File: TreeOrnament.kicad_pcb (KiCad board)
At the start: 2 copper layers, 80 x 99 mm, 44 parts, among them J1 USB_B_Micro

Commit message: Use newer version of Micro B footprint.
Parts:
- J1: footprint myLibrary:USB_Micro-B_Wuerth-614105150721_CircularHoles -> myLibrary:USB_Micro-B_Wuerth-614105150721_Vertical_CircularHoles

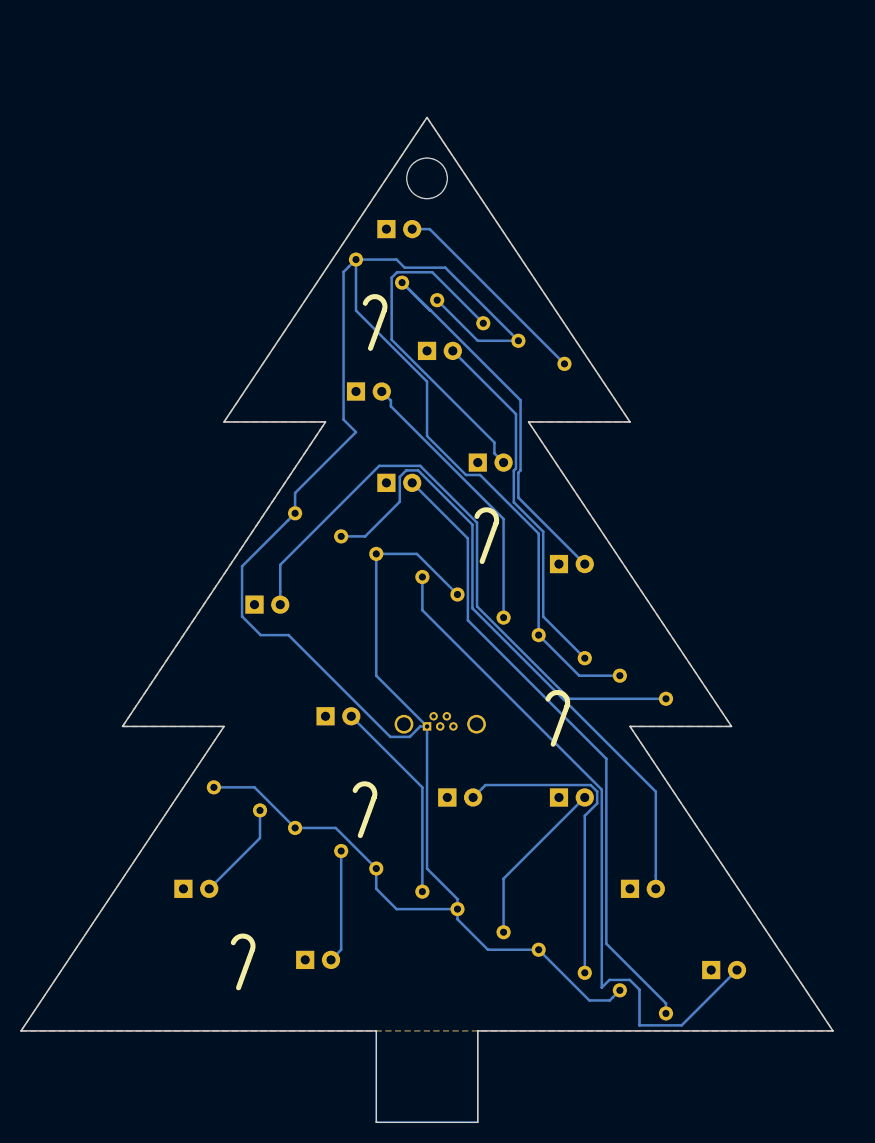
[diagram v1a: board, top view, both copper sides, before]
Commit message: Flip the board over.
(This way the customer ID will be on the "back" instead of the "front".)
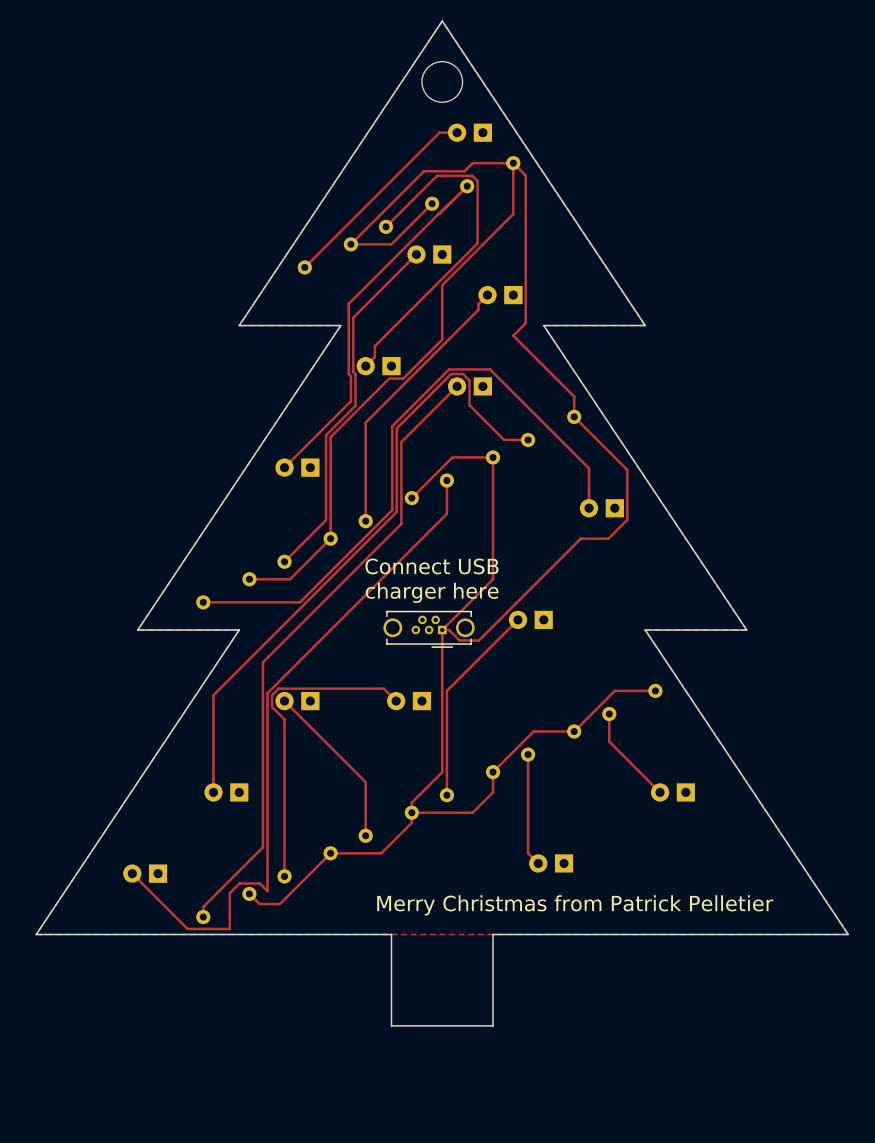
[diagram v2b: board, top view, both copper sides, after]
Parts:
- D1, D10, D11, D12, D13, D14, D2, D3, D4, D5, D6, D7, D8, D9, R1, R10, R11, R12, R13, R14, R2, R3, R4, R5, R6, R7, R8, R9, REF** (x15): moved to B.Cu
- J1: moved to F.Cu
- moved REF** 60.3 mm to (165.5, 105.5), turned to 180 degrees
- moved D8 55.3 mm to (108.5, 104.5), turned to 180 degrees
- moved D1 50.4 mm to (160.5, 96.5), turned to 180 degrees
- moved R1 44.5 mm to (157.5, 86.5), turned to 206.6 degrees
- moved REF** 40.6 mm to (155.5, 104.5), turned to 200 degrees
- moved D7 39.7 mm to (116.5, 96.5), turned to 180 degrees
- moved R11 37.7 mm to (117.5, 75.5), turned to 206.6 degrees
- moved R6 37.7 mm to (117.5, 106.5), turned to 206.6 degrees
- moved D11 36.7 mm to (153.5, 68.5), turned to 180 degrees
- moved REF** 36.7 mm to (153.5, 76.5), turned to 180 degrees
- moved R2 29.1 mm to (149.5, 90.5), turned to 206.6 degrees
- moved R7 29.1 mm to (149.5, 59.5), turned to 206.6 degrees
- moved D2 27.2 mm to (148.5, 103.5), turned to 180 degrees
- moved D12 26.3 mm to (123.5, 64.5), turned to 180 degrees
- moved D4 26.3 mm to (123.5, 87.5), turned to 180 degrees
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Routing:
- added copper zone on F.Cu, net +5V
- added copper zone on B.Cu, net GND
- removed copper zone on B.Cu, net +5V
- removed copper zone on F.Cu, net GND

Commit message: Change signature text to include the year again.
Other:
- board text added: "Patrick Pelletier / Christmas 2017"
- board text removed: "Merry Christmas from Patrick Pelletier"
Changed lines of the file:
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@@
   )
   (page USLetter)
+  (title_block
+    (title "Christmas Tree Ornament")
+    (date 2017-10-31)
+    (rev 1.1)
+    (company "Patrick Pelletier")
+  )
   (layers
     (0 F.Cu signal)
@@
   (gr_line (start 131.5 119.5) (end 131.5 110.5) (angle 90) (layer Edge.Cuts) (width 0.15))
   (gr_line (start 141.5 110.5) (end 141.5 119.5) (angle 90) (layer Edge.Cuts) (width 0.15))
-  (gr_text "Merry Christmas from Patrick Pelletier" (at 149.5 107.5) (layer F.SilkS)
+  (gr_text "Patrick Pelletier / Christmas 2017" (at 134 93 26.6) (layer F.SilkS)
     (effects (font (size 1.5 1.5) (thickness 0.3)))
   )

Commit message: Add some optional SMT decoupling caps.
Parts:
- added C1: 3.3uF, Capacitors_SMD:C_0805_HandSoldering, F.Cu at (144.0, 44.0)
- added C2: 3.3uF, Capacitors_SMD:C_0805_HandSoldering, F.Cu at (122.0, 68.0)
- added C3: 3.3uF, Capacitors_SMD:C_0805_HandSoldering, F.Cu at (153.0, 104.0)
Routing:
- net +5V: track 247.1 -> 271.4 mm
- net GND: track 0.00 -> 10.9 mm
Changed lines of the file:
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@@
 (kicad_pcb (version 4) (host pcbnew 4.0.7)
   (general
-    (links 44)
+    (links 50)
     (no_connects 0)
-    (area 94.924999 29.924999 175.075001 131.075)
+    (area 96.424999 20.424999 176.575001 121.575)
     (thickness 1.6)
     (drawings 17)
-    (tracks 131)
+    (tracks 141)
     (zones 0)
-    (modules 44)
+    (modules 47)
     (nets 20)
   )
@@
   (title_block
     (title "Christmas Tree Ornament")
-    (date 2017-10-31)
+    (date 2017-11-02)
     (rev 1.1)
     (company "Patrick Pelletier")
@@
     )
   )
+  (module Capacitors_SMD:C_0805_HandSoldering (layer F.Cu)
+    (at 144 44 180)
+    (descr "Capacitor SMD 0805, hand soldering")
+    (tags "capacitor 0805")
+    (attr smd)
+    (fp_text reference C1 (at 0 -1.75 180) (layer F.SilkS) hide
+      (effects (font (size 1 1) (thickness 0.15)))
+    )
+    (fp_text value 3.3uF (at 0 1.75 180) (layer F.Fab)
+      (effects (font (size 1 1) (thickness 0.15)))
+    )
+    (fp_text user %R (at 0 -1.75 180) (layer F.Fab)
+      (effects (font (size 1 1) (thickness 0.15)))
+    )
+    (fp_line (start -1 0.62) (end -1 -0.62) (layer F.Fab) (width 0.1))
+    (fp_line (start 1 0.62) (end -1 0.62) (layer F.Fab) (width 0.1))
+    (fp_line (start 1 -0.62) (end 1 0.62) (layer F.Fab) (width 0.1))
+    (fp_line (start -1 -0.62) (end 1 -0.62) (layer F.Fab) (width 0.1))
+    (fp_line (start 0.5 -0.85) (end -0.5 -0.85) (layer F.SilkS) (width 0.12))
+    (fp_line (start -0.5 0.85) (end 0.5 0.85) (layer F.SilkS) (width 0.12))
+    (fp_line (start -2.25 -0.88) (end 2.25 -0.88) (layer F.CrtYd) (width 0.05))
+    (fp_line (start -2.25 -0.88) (end -2.25 0.87) (layer F.CrtYd) (width 0.05))
+    (fp_line (start 2.25 0.87) (end 2.25 -0.88) (layer F.CrtYd) (width 0.05))
+    (fp_line (start 2.25 0.87) (end -2.25 0.87) (layer F.CrtYd) (width 0.05))
+    (pad 1 smd rect (at -1.25 0 180) (size 1.5 1.25) (layers F.Cu F.Paste F.Mask)
+      (net 10 +5V))
+    (pad 2 smd rect (at 1.25 0 180) (size 1.5 1.25) (layers F.Cu F.Paste F.Mask)
+      (net 1 GND))
+    (model Capacitors_SMD.3dshapes/C_0805.wrl
+      (at (xyz 0 0 0))
+      (scale (xyz 1 1 1))
+      (rotate (xyz 0 0 0))
+    )
+  )
+  (module Capacitors_SMD:C_0805_HandSoldering (layer F.Cu)
+    (at 122 68)
+    (descr "Capacitor SMD 0805, hand soldering")
+    (tags "capacitor 0805")
+    (attr smd)
+    (fp_text reference C2 (at 0 -1.75) (layer F.SilkS) hide
+      (effects (font (size 1 1) (thickness 0.15)))
+    )
+    (fp_text value 3.3uF (at 0 1.75) (layer F.Fab)
+      (effects (font (size 1 1) (thickness 0.15)))
+    )
+    (fp_text user %R (at 0 -1.75) (layer F.Fab)
+      (effects (font (size 1 1) (thickness 0.15)))
+    )
+    (fp_line (start -1 0.62) (end -1 -0.62) (layer F.Fab) (width 0.1))
+    (fp_line (start 1 0.62) (end -1 0.62) (layer F.Fab) (width 0.1))
+    (fp_line (start 1 -0.62) (end 1 0.62) (layer F.Fab) (width 0.1))
+    (fp_line (start -1 -0.62) (end 1 -0.62) (layer F.Fab) (width 0.1))
+    (fp_line (start 0.5 -0.85) (end -0.5 -0.85) (layer F.SilkS) (width 0.12))
+    (fp_line (start -0.5 0.85) (end 0.5 0.85) (layer F.SilkS) (width 0.12))
+    (fp_line (start -2.25 -0.88) (end 2.25 -0.88) (layer F.CrtYd) (width 0.05))
+    (fp_line (start -2.25 -0.88) (end -2.25 0.87) (layer F.CrtYd) (width 0.05))
+    (fp_line (start 2.25 0.87) (end 2.25 -0.88) (layer F.CrtYd) (width 0.05))
+    (fp_line (start 2.25 0.87) (end -2.25 0.87) (layer F.CrtYd) (width 0.05))
+    (pad 1 smd rect (at -1.25 0) (size 1.5 1.25) (layers F.Cu F.Paste F.Mask)
+      (net 10 +5V))
+    (pad 2 smd rect (at 1.25 0) (size 1.5 1.25) (layers F.Cu F.Paste F.Mask)
+      (net 1 GND))
+    (model Capacitors_SMD.3dshapes/C_0805.wrl
+      (at (xyz 0 0 0))
+      (scale (xyz 1 1 1))
+      (rotate (xyz 0 0 0))
+    )
+  )
+  (module Capacitors_SMD:C_0805_HandSoldering (layer F.Cu)
+    (at 153 104 180)
+    (descr "Capacitor SMD 0805, hand soldering")
+    (tags "capacitor 0805")
+    (attr smd)
+    (fp_text reference C3 (at 0 -1.75 180) (layer F.SilkS) hide
+      (effects (font (size 1 1) (thickness 0.15)))
+    )
+    (fp_text value 3.3uF (at 0 1.75 180) (layer F.Fab)
+      (effects (font (size 1 1) (thickness 0.15)))
+    )
+    (fp_text user %R (at 0 -1.75 180) (layer F.Fab)
+      (effects (font (size 1 1) (thickness 0.15)))
+    )
+    (fp_line (start -1 0.62) (end -1 -0.62) (layer F.Fab) (width 0.1))
+    (fp_line (start 1 0.62) (end -1 0.62) (layer F.Fab) (width 0.1))
+    (fp_line (start 1 -0.62) (end 1 0.62) (layer F.Fab) (width 0.1))
+    (fp_line (start -1 -0.62) (end 1 -0.62) (layer F.Fab) (width 0.1))
+    (fp_line (start 0.5 -0.85) (end -0.5 -0.85) (layer F.SilkS) (width 0.12))
+    (fp_line (start -0.5 0.85) (end 0.5 0.85) (layer F.SilkS) (width 0.12))
+    (fp_line (start -2.25 -0.88) (end 2.25 -0.88) (layer F.CrtYd) (width 0.05))
+    (fp_line (start -2.25 -0.88) (end -2.25 0.87) (layer F.CrtYd) (width 0.05))
+    (fp_line (start 2.25 0.87) (end 2.25 -0.88) (layer F.CrtYd) (width 0.05))
+    (fp_line (start 2.25 0.87) (end -2.25 0.87) (layer F.CrtYd) (width 0.05))
+    (pad 1 smd rect (at -1.25 0 180) (size 1.5 1.25) (layers F.Cu F.Paste F.Mask)
+      (net 10 +5V))
+    (pad 2 smd rect (at 1.25 0 180) (size 1.5 1.25) (layers F.Cu F.Paste F.Mask)
+      (net 1 GND))
+    (model Capacitors_SMD.3dshapes/C_0805.wrl
+      (at (xyz 0 0 0))
+      (scale (xyz 1 1 1))
+      (rotate (xyz 0 0 0))
+    )
+  )
   (gr_line (start 131.5 119.5) (end 131.5 110.5) (angle 90) (layer Edge.Cuts) (width 0.15))
   (gr_line (start 141.5 110.5) (end 141.5 119.5) (angle 90) (layer Edge.Cuts) (width 0.15))
@@
   (gr_line (start 156.5 50.5) (end 146.5 50.5) (angle 90) (layer Edge.Cuts) (width 0.15))
   (gr_line (start 136.5 20.5) (end 156.5 50.5) (angle 90) (layer Edge.Cuts) (width 0.15))
+  (segment (start 151.75 104) (end 149 104) (width 0.25) (layer F.Cu) (net 1))
+  (segment (start 149 104) (end 148.5 103.5) (width 0.25) (layer F.Cu) (net 1))
+  (segment (start 123.25 68) (end 123.25 64.75) (width 0.25) (layer F.Cu) (net 1))
+  (segment (start 123.25 64.75) (end 123.5 64.5) (width 0.25) (layer F.Cu) (net 1))
+  (segment (start 142.75 44) (end 142.75 46.75) (width 0.25) (layer F.Cu) (net 1))
+  (segment (start 142.75 46.75) (end 143.5 47.5) (width 0.25) (layer F.Cu) (net 1))
   (segment (start 152.957696 88.774616) (end 152.957696 91.497696) (width 0.25) (layer F.Cu) (net 2))
   (segment (start 152.957696 91.497696) (end 157.96 96.5) (width 0.25) (layer F.Cu) (net 2))
@@
   (segment (start 116.525001 105.474999) (end 118.527973 105.474999) (width 0.25) (layer F.Cu) (net 9))
   (segment (start 118.527973 105.474999) (end 119.284988 106.232014) (width 0.25) (layer F.Cu) (net 9))
+  (segment (start 154.25 104) (end 154.25 95.25) (width 0.25) (layer F.Cu) (net 10))
+  (segment (start 154.25 95.25) (end 149.5 90.5) (width 0.25) (layer F.Cu) (net 10))
+  (segment (start 120.75 68) (end 120.75 72.25) (width 0.25) (layer F.Cu) (net 10))
+  (segment (start 120.75 72.25) (end 117.5 75.5) (width 0.25) (layer F.Cu) (net 10))
   (segment (start 133.5 67.5) (end 137.5 63.5) (width 0.25) (layer F.Cu) (net 10))
   (segment (start 137.5 63.5) (end 141.5 63.5) (width 0.25) (layer F.Cu) (net 10))

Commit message: label USB port as being Micro B
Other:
- board text added: "Micro B"
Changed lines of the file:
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@@
     (area 96.424999 20.424999 176.575001 121.575)
     (thickness 1.6)
-    (drawings 17)
+    (drawings 18)
     (tracks 141)
     (zones 0)
@@
     )
   )
+  (gr_text "Micro B" (at 135 83.5) (layer F.SilkS)
+    (effects (font (size 1 1) (thickness 0.2)))
+  )
   (gr_line (start 131.5 119.5) (end 131.5 110.5) (angle 90) (layer Edge.Cuts) (width 0.15))

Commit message: Change resistor value from 150 to 1k.
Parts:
- R1, R10, R11, R12, R13, R14, R2, R3, R4, R5, R6, R7, R8, R9: value 150 -> 1k
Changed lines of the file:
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@@
     (links 50)
     (no_connects 0)
-    (area 96.424999 20.424999 176.575001 121.575)
+    (area 96.424999 20.424999 176.575001 119.575001)
     (thickness 1.6)
     (drawings 18)
@@
   (title_block
     (title "Christmas Tree Ornament")
-    (date 2017-11-02)
-    (rev 1.1)
+    (date 2017-11-25)
+    (rev 1.2)
     (company "Patrick Pelletier")
   )
@@
       (effects (font (size 1 1) (thickness 0.15)) (justify mirror))
     )
-    (fp_text value 150 (at 2.54 -1.86 206.6) (layer B.Fab) hide
+    (fp_text value 1k (at 2.54 -1.86 206.6) (layer B.Fab) hide
       (effects (font (size 1 1) (thickness 0.15)) (justify mirror))
     )
@@
       (effects (font (size 1 1) (thickness 0.15)) (justify mirror))
     )
-    (fp_text value 150 (at 2.54 -1.86 206.6) (layer B.Fab) hide
+    (fp_text value 1k (at 2.54 -1.86 206.6) (layer B.Fab) hide
       (effects (font (size 1 1) (thickness 0.15)) (justify mirror))
     )
@@
       (effects (font (size 1 1) (thickness 0.15)) (justify mirror))
     )
-    (fp_text value 150 (at 2.54 -1.86 206.6) (layer B.Fab) hide
+    (fp_text value 1k (at 2.54 -1.86 206.6) (layer B.Fab) hide
       (effects (font (size 1 1) (thickness 0.15)) (justify mirror))
     )
@@
       (effects (font (size 1 1) (thickness 0.15)) (justify mirror))
     )
-    (fp_text value 150 (at 2.54 -1.86 206.6) (layer B.Fab) hide
+    (fp_text value 1k (at 2.54 -1.86 206.6) (layer B.Fab) hide
       (effects (font (size 1 1) (thickness 0.15)) (justify mirror))
     )
@@
       (effects (font (size 1 1) (thickness 0.15)) (justify mirror))
     )
-    (fp_text value 150 (at 2.54 -1.86 206.6) (layer B.Fab) hide
+    (fp_text value 1k (at 2.54 -1.86 206.6) (layer B.Fab) hide
       (effects (font (size 1 1) (thickness 0.15)) (justify mirror))
     )
@@
       (effects (font (size 1 1) (thickness 0.15)) (justify mirror))
     )
-    (fp_text value 150 (at 2.54 -1.86 206.6) (layer B.Fab) hide
+    (fp_text value 1k (at 2.54 -1.86 206.6) (layer B.Fab) hide
       (effects (font (size 1 1) (thickness 0.15)) (justify mirror))
     )
@@
       (effects (font (size 1 1) (thickness 0.15)) (justify mirror))
     )
-    (fp_text value 150 (at 2.54 -1.86 206.6) (layer B.Fab) hide
+    (fp_text value 1k (at 2.54 -1.86 206.6) (layer B.Fab) hide
       (effects (font (size 1 1) (thickness 0.15)) (justify mirror))
     )
@@
       (effects (font (size 1 1) (thickness 0.15)) (justify mirror))
     )
-    (fp_text value 150 (at 2.54 -1.86 206.6) (layer B.Fab) hide
+    (fp_text value 1k (at 2.54 -1.86 206.6) (layer B.Fab) hide
       (effects (font (size 1 1) (thickness 0.15)) (justify mirror))
     )
@@
       (effects (font (size 1 1) (thickness 0.15)) (justify mirror))
     )
-    (fp_text value 150 (at 2.54 -1.86 206.6) (layer B.Fab) hide
+    (fp_text value 1k (at 2.54 -1.86 206.6) (layer B.Fab) hide
       (effects (font (size 1 1) (thickness 0.15)) (justify mirror))
     )
@@
       (effects (font (size 1 1) (thickness 0.15)) (justify mirror))
     )
-    (fp_text value 150 (at 2.54 -1.86 206.6) (layer B.Fab) hide
+    (fp_text value 1k (at 2.54 -1.86 206.6) (layer B.Fab) hide
       (effects (font (size 1 1) (thickness 0.15)) (justify mirror))
     )
@@
       (effects (font (size 1 1) (thickness 0.15)) (justify mirror))
     )
-    (fp_text value 150 (at 2.54 -1.86 206.6) (layer B.Fab) hide
+    (fp_text value 1k (at 2.54 -1.86 206.6) (layer B.Fab) hide
       (effects (font (size 1 1) (thickness 0.15)) (justify mirror))
     )
@@
       (effects (font (size 1 1) (thickness 0.15)) (justify mirror))
     )
-    (fp_text value 150 (at 2.54 -1.86 206.6) (layer B.Fab) hide
+    (fp_text value 1k (at 2.54 -1.86 206.6) (layer B.Fab) hide
       (effects (font (size 1 1) (thickness 0.15)) (justify mirror))
     )
@@
       (effects (font (size 1 1) (thickness 0.15)) (justify mirror))
     )
-    (fp_text value 150 (at 2.54 -1.86 206.6) (layer B.Fab) hide
+    (fp_text value 1k (at 2.54 -1.86 206.6) (layer B.Fab) hide
       (effects (font (size 1 1) (thickness 0.15)) (justify mirror))
     )
@@
       (effects (font (size 1 1) (thickness 0.15)) (justify mirror))
     )
-    (fp_text value 150 (at 2.54 -1.86 206.6) (layer B.Fab) hide
-      (effects (font (size 1 1) (thickness 0.15)) (justify mirror))
-    )
+    (fp_text value 1k (at 2.54 -1.86 206.6) (layer B.Fab) hide
+      (effects (font (size 1 1) (thickness 0.15)) (justify mirror))
+    )

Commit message: Add github URL and KiCad logo.
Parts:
- added REF***: KiCad-Logo2_6mm_SilkScreen, Symbols:KiCad-Logo2_6mm_SilkScreen, F.Cu at (136.2, 105.5)
- added REF***: OSHW-Logo_5.7x6mm_SilkScreen, Symbols:OSHW-Logo_5.7x6mm_SilkScreen, F.Cu at (164.2, 105.5)
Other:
- board text added: "https://github.com/ppelleti/TreeOrnament"
- board text removed: "Patrick Pelletier / Christmas 2017"
